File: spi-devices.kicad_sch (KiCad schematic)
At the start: 15 parts, among them U5 IIM-42652, U8 ICE5LP1K-SG48

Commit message: Checkpoint
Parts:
- C26: value (none) -> C_10u_0603; footprint (none) -> jetson-nano-baseboard-footprints:0603-cap
- C27: value (none) -> C_100n_0402; footprint (none) -> jetson-nano-baseboard-footprints:0402-cap
- D7: value (none) -> diode
- FB4: value (none) -> 100; footprint (none) -> jetson-nano-baseboard-footprints:0603-res
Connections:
- net IMU-INT1: now also U8.9 (IOB_16a)
- net IMU-INT2: now also U8.6 (IOB_13b)
- net SPI-CIPO: no longer U8.16 (IOB_35b_SPI_SS)
- net SPI-COPI: now also U8.17 (IOB_33b_SPI_SI)
- net SPI-SCK: now also U8.15 (IOB_34a_SPI_SCK); no longer U8.17 (IOB_33b_SPI_SI)
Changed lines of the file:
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@@
+    (stroke (width 0) (type default) (color 0 0 0 0))
+  )
+  (wire (pts (xy 226.06 90.17) (xy 232.41 90.17))
     (stroke (width 0) (type default) (color 0 0 0 0))
   )
@@
     (stroke (width 0) (type default) (color 0 0 0 0))
   )
+  (wire (pts (xy 215.9 59.69) (xy 232.41 59.69))
+    (stroke (width 0) (type default) (color 0 0 0 0))
+  )
   (wire (pts (xy 229.87 137.16) (xy 246.38 137.16))
     (stroke (width 0) (type default) (color 0 0 0 0))
@@
     (stroke (width 0) (type default) (color 0 0 0 0))
   )
-  (wire (pts (xy 44.45 68.58) (xy 52.07 68.58))
+  (wire (pts (xy 35.56 68.58) (xy 52.07 68.58))
+    (stroke (width 0) (type default) (color 0 0 0 0))
+  )
+  (wire (pts (xy 226.06 87.63) (xy 232.41 87.63))
     (stroke (width 0) (type default) (color 0 0 0 0))
   )
@@
     (stroke (width 0) (type default) (color 0 0 0 0))
   )
-  (wire (pts (xy 44.45 71.12) (xy 52.07 71.12))
+  (wire (pts (xy 35.56 71.12) (xy 52.07 71.12))
     (stroke (width 0) (type default) (color 0 0 0 0))
   )
@@
     (stroke (width 0) (type default) (color 0 0 0 0))
   )
+  (wire (pts (xy 215.9 62.23) (xy 232.41 62.23))
+    (stroke (width 0) (type default) (color 0 0 0 0))
+  )
   (wire (pts (xy 80.01 58.42) (xy 74.93 58.42))
     (stroke (width 0) (type default) (color 0 0 0 0))
@@
     (stroke (width 0) (type default) (color 0 0 0 0))
   )
-  (wire (pts (xy 226.06 87.63) (xy 232.41 87.63))
-    (stroke (width 0) (type default) (color 0 0 0 0))
-  )
   (wire (pts (xy 242.316 134.62) (xy 242.316 139.7))
     (stroke (width 0) (type default) (color 0 0 0 0))
@@
   (wire (pts (xy 235.712 134.62) (xy 242.316 134.62))
     (stroke (width 0) (type default) (color 0 0 0 0))
+  )
+  (label "IMU-INT2" (at 215.9 59.69 0)
+    (effects (font (size 1.27 1.27)) (justify left bottom))
+  )
+  (label "IMU-INT1" (at 215.9 62.23 0)
+    (effects (font (size 1.27 1.27)) (justify left bottom))
+  )
+  (label "IMU-INT2" (at 35.56 71.12 0)
+    (effects (font (size 1.27 1.27)) (justify left bottom))
   )
   (label "VCCPLL" (at 237.236 134.62 0)
     (effects (font (size 1.27 1.27)) (justify left bottom))
   )
+  (label "IMU-INT1" (at 35.56 68.58 0)
+    (effects (font (size 1.27 1.27)) (justify left bottom))
+  )
   (label "VPP2V5" (at 245.618 154.94 0)
     (effects (font (size 1.27 1.27)) (justify left bottom))
-  )
-  (global_label "IMU-INT1" (shape bidirectional) (at 44.45 68.58 180) (fields_autoplaced)
-    (effects (font (size 1.27 1.27)) (justify right))
-    (property "Intersheet References" "${INTERSHEET_REFS}" (id 0) (at 33.0544 68.5006 0)
-      (effects (font (size 1.27 1.27)) (justify right) hide)
-    )
   )
   (global_label "SPI-CIPO" (shape input) (at 44.45 55.88 180) (fields_autoplaced)
@@
     )
   )
-  (global_label "SPI-SCK" (shape input) (at 226.06 87.63 180) (fields_autoplaced)
-    (effects (font (size 1.27 1.27)) (justify right))
-    (property "Intersheet References" "${INTERSHEET_REFS}" (id 0) (at 215.3296 87.5506 0)
+  (global_label "SPI-SCK" (shape input) (at 226.06 90.17 180) (fields_autoplaced)
+    (effects (font (size 1.27 1.27)) (justify right))
+    (property "Intersheet References" "${INTERSHEET_REFS}" (id 0) (at 215.3296 90.0906 0)
       (effects (font (size 1.27 1.27)) (justify right) hide)
     )
@@
     )
   )
-  (global_label "CAM4-IO0" (shape output) (at 225.044 61.976 180) (fields_autoplaced)
-    (effects (font (size 1.27 1.27)) (justify right))
-    (property "Intersheet References" "${INTERSHEET_REFS}" (id 0) (at 212.9831 61.8966 0)
+  (global_label "CAM4-IO0" (shape output) (at 226.314 67.818 180) (fields_autoplaced)
+    (effects (font (size 1.27 1.27)) (justify right))
+    (property "Intersheet References" "${INTERSHEET_REFS}" (id 0) (at 214.2531 67.7386 0)
       (effects (font (size 1.27 1.27)) (justify right) hide)
     )
@@
     )
   )
-  (global_label "IMU-INT2" (shape bidirectional) (at 44.45 71.12 180) (fields_autoplaced)
-    (effects (font (size 1.27 1.27)) (justify right))
-    (property "Intersheet References" "${INTERSHEET_REFS}" (id 0) (at 33.0544 71.0406 0)
-      (effects (font (size 1.27 1.27)) (justify right) hide)
-    )
-  )
   (global_label "SPI-SCK" (shape input) (at 44.45 60.96 180) (fields_autoplaced)
     (effects (font (size 1.27 1.27)) (justify right))
@@
     )
   )
-  (global_label "SPI-CIPO" (shape input) (at 226.0912 92.71 180) (fields_autoplaced)
-    (effects (font (size 1.27 1.27)) (justify right))
-    (property "Intersheet References" "${INTERSHEET_REFS}" (id 0) (at 214.6351 92.6306 0)
+  (global_label "SPI-COPI" (shape input) (at 226.06 87.63 180) (fields_autoplaced)
+    (effects (font (size 1.27 1.27)) (justify right))
+    (property "Intersheet References" "${INTERSHEET_REFS}" (id 0) (at 214.6039 87.5506 0)
       (effects (font (size 1.27 1.27)) (justify right) hide)
     )
@@
     )
   )
-  (global_label "CAM4-IO1" (shape output) (at 225.044 64.516 180) (fields_autoplaced)
-    (effects (font (size 1.27 1.27)) (justify right))
-    (property "Intersheet References" "${INTERSHEET_REFS}" (id 0) (at 212.9831 64.4366 0)
+  (global_label "CAM4-IO1" (shape output) (at 226.314 70.358 180) (fields_autoplaced)
+    (effects (font (size 1.27 1.27)) (justify right))
+    (property "Intersheet References" "${INTERSHEET_REFS}" (id 0) (at 214.2531 70.2786 0)
       (effects (font (size 1.27 1.27)) (justify right) hide)
     )
@@
       (effects (font (size 1.524 1.524)) (justify left))
     )
-    (property "Value" "" (id 1) (at 242.316 139.7 0)
-      (effects (font (size 1.524 1.524)) hide)
-    )
-    (property "Footprint" "" (id 2) (at 237.236 148.59 0)
+    (property "Value" "C_100n_0402" (id 1) (at 242.316 139.7 0)
+      (effects (font (size 1.524 1.524)) hide)
+    )
+    (property "Footprint" "jetson-nano-baseboard-footprints:0402-cap" (id 2) (at 237.236 148.59 0)
       (effects (font (size 1.524 1.524)) (justify left) hide)
     )
@@
       (effects (font (size 1.524 1.524)) (justify left))
     )
-    (property "Value" "" (id 1) (at 235.712 139.7 0)
-      (effects (font (size 1.524 1.524)) hide)
-    )
-    (property "Footprint" "" (id 2) (at 230.632 148.59 0)
+    (property "Value" "C_10u_0603" (id 1) (at 235.712 139.7 0)
+      (effects (font (size 1.524 1.524)) hide)
+    )
+    (property "Footprint" "jetson-nano-baseboard-footprints:0603-cap" (id 2) (at 230.632 148.59 0)
       (effects (font (size 1.524 1.524)) (justify left) hide)
     )
@@
       (effects (font (size 1.524 1.524)))
     )
-    (property "Value" "" (id 1) (at 242.824 156.464 90)
+    (property "Value" "diode" (id 1) (at 242.824 156.464 90)
       (effects (font (size 1.524 1.524)))
     )
@@
     (in_bom yes) (on_board yes)
     (property "Reference" "FB4" (id 0) (at 225.0059 133.35 90))
-    (property "Value" "" (id 1) (at 230.8479 133.604 90))
-    (property "Footprint" "" (id 2) (at 227.33 136.398 90)
-      (effects (font (size 1.27 1.27)) hide)
-    )
+    (property "Value" "100" (id 1) (at 230.8479 133.604 90))
+    (property "Footprint" "jetson-nano-baseboard-footprints:0603-res" (id 2) (at 227.33 136.398 90)
+      (effects (font (size 1.27 1.27)) hide)
+    )

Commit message: Checkpoint
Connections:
- net CAM0-IO0: now also U8.44 (IOB_3b_G6); no longer U8.46 (IOB_0a)
- net CAM0-IO1: now also U8.45 (IOB_5b); no longer U8.47 (IOB_2a)
- net CAM1-IO0: now also U8.47 (IOB_2a); no longer U8.44 (IOB_3b_G6)
- net CAM1-IO1: now also U8.46 (IOB_0a); no longer U8.48 (IOB_4a)
- net CAM2-IO0: now also U8.4 (IOB_8a); no longer U8.45 (IOB_5b)
- net CAM2-IO1: now also U8.3 (IOB_9b); no longer U8.2 (IOB_6a)
- net CAM3-IO0: now also U8.2 (IOB_6a); no longer U8.4 (IOB_8a)
- net CAM3-IO1: now also U8.48 (IOB_4a); no longer U8.3 (IOB_9b)
- net CAM4-IO0: now also U8.9 (IOB_16a)
- net CAM4-IO1: now also U8.10 (IOB_18a)
- net IMU-INT1: now also U8.12 (IOB_22b); no longer U8.9 (IOB_16a)
- net IMU-INT2: now also U8.11 (IOB_20a); no longer U8.6 (IOB_13b)
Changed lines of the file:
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@@
+    (stroke (width 0) (type default) (color 0 0 0 0))
+  )
+  (wire (pts (xy 222.504 64.77) (xy 232.41 64.77))
     (stroke (width 0) (type default) (color 0 0 0 0))
   )
@@
     (stroke (width 0) (type default) (color 0 0 0 0))
   )
+  (wire (pts (xy 222.504 62.23) (xy 232.41 62.23))
+    (stroke (width 0) (type default) (color 0 0 0 0))
+  )
   (wire (pts (xy 97.155 52.705) (xy 97.155 54.61))
     (stroke (width 0) (type default) (color 0 0 0 0))
@@
     (stroke (width 0) (type default) (color 0 0 0 0))
   )
-  (wire (pts (xy 215.9 59.69) (xy 232.41 59.69))
+  (wire (pts (xy 223.012 67.31) (xy 232.41 67.31))
     (stroke (width 0) (type default) (color 0 0 0 0))
   )
@@
     (stroke (width 0) (type default) (color 0 0 0 0))
   )
-  (wire (pts (xy 215.9 62.23) (xy 232.41 62.23))
+  (wire (pts (xy 223.012 69.85) (xy 232.41 69.85))
     (stroke (width 0) (type default) (color 0 0 0 0))
   )
@@
     (stroke (width 0) (type default) (color 0 0 0 0))
   )
-  (label "IMU-INT2" (at 215.9 59.69 0)
-    (effects (font (size 1.27 1.27)) (justify left bottom))
-  )
-  (label "IMU-INT1" (at 215.9 62.23 0)
+  (label "IMU-INT2" (at 223.012 67.31 0)
+    (effects (font (size 1.27 1.27)) (justify left bottom))
+  )
+  (label "IMU-INT1" (at 223.012 69.85 0)
     (effects (font (size 1.27 1.27)) (justify left bottom))
   )
@@
     )
   )
-  (global_label "CAM2-IO0" (shape output) (at 167.64 133.35 180) (fields_autoplaced)
-    (effects (font (size 1.27 1.27)) (justify right))
-    (property "Intersheet References" "${INTERSHEET_REFS}" (id 0) (at 155.5791 133.2706 0)
-      (effects (font (size 1.27 1.27)) (justify right) hide)
-    )
-  )
-  (global_label "CAM3-IO1" (shape output) (at 167.64 140.97 180) (fields_autoplaced)
-    (effects (font (size 1.27 1.27)) (justify right))
-    (property "Intersheet References" "${INTERSHEET_REFS}" (id 0) (at 155.5791 140.8906 0)
-      (effects (font (size 1.27 1.27)) (justify right) hide)
-    )
-  )
-  (global_label "CAM3-IO0" (shape output) (at 167.64 138.43 180) (fields_autoplaced)
+  (global_label "CAM2-IO0" (shape output) (at 167.64 138.43 180) (fields_autoplaced)
     (effects (font (size 1.27 1.27)) (justify right))
     (property "Intersheet References" "${INTERSHEET_REFS}" (id 0) (at 155.5791 138.3506 0)
+      (effects (font (size 1.27 1.27)) (justify right) hide)
+    )
+  )
+  (global_label "CAM3-IO1" (shape output) (at 167.64 130.81 180) (fields_autoplaced)
+    (effects (font (size 1.27 1.27)) (justify right))
+    (property "Intersheet References" "${INTERSHEET_REFS}" (id 0) (at 155.5791 130.7306 0)
+      (effects (font (size 1.27 1.27)) (justify right) hide)
+    )
+  )
+  (global_label "CAM3-IO0" (shape output) (at 167.64 135.89 180) (fields_autoplaced)
+    (effects (font (size 1.27 1.27)) (justify right))
+    (property "Intersheet References" "${INTERSHEET_REFS}" (id 0) (at 155.5791 135.8106 0)
       (effects (font (size 1.27 1.27)) (justify right) hide)
     )
@@
     )
   )
-  (global_label "CAM4-IO0" (shape output) (at 226.314 67.818 180) (fields_autoplaced)
-    (effects (font (size 1.27 1.27)) (justify right))
-    (property "Intersheet References" "${INTERSHEET_REFS}" (id 0) (at 214.2531 67.7386 0)
-      (effects (font (size 1.27 1.27)) (justify right) hide)
-    )
-  )
-  (global_label "CAM2-IO1" (shape output) (at 167.64 135.89 180) (fields_autoplaced)
-    (effects (font (size 1.27 1.27)) (justify right))
-    (property "Intersheet References" "${INTERSHEET_REFS}" (id 0) (at 155.5791 135.8106 0)
+  (global_label "CAM4-IO0" (shape output) (at 222.504 62.23 180) (fields_autoplaced)
+    (effects (font (size 1.27 1.27)) (justify right))
+    (property "Intersheet References" "${INTERSHEET_REFS}" (id 0) (at 210.4431 62.1506 0)
+      (effects (font (size 1.27 1.27)) (justify right) hide)
+    )
+  )
+  (global_label "CAM2-IO1" (shape output) (at 167.64 140.97 180) (fields_autoplaced)
+    (effects (font (size 1.27 1.27)) (justify right))
+    (property "Intersheet References" "${INTERSHEET_REFS}" (id 0) (at 155.5791 140.8906 0)
       (effects (font (size 1.27 1.27)) (justify right) hide)
     )
@@
     )
   )
-  (global_label "CAM0-IO0" (shape output) (at 167.64 123.19 180) (fields_autoplaced)
+  (global_label "CAM0-IO0" (shape output) (at 167.64 128.27 180) (fields_autoplaced)
+    (effects (font (size 1.27 1.27)) (justify right))
+    (property "Intersheet References" "${INTERSHEET_REFS}" (id 0) (at 155.5791 128.1906 0)
+      (effects (font (size 1.27 1.27)) (justify right) hide)
+    )
+  )
+  (global_label "CAM-VIO" (shape input) (at 180.34 106.68 180) (fields_autoplaced)
+    (effects (font (size 1.27 1.27)) (justify right))
+    (property "Intersheet References" "${INTERSHEET_REFS}" (id 0) (at 169.6096 106.7594 0)
+      (effects (font (size 1.27 1.27)) (justify right) hide)
+    )
+  )
+  (global_label "ICE-RESET" (shape input) (at 226.06 52.07 180) (fields_autoplaced)
+    (effects (font (size 1.27 1.27)) (justify right))
+    (property "Intersheet References" "${INTERSHEET_REFS}" (id 0) (at 213.3944 51.9906 0)
+      (effects (font (size 1.27 1.27)) (justify right) hide)
+    )
+  )
+  (global_label "3V3_SYS" (shape input) (at 226.06 38.1 180) (fields_autoplaced)
+    (effects (font (size 1.27 1.27)) (justify right))
+    (property "Intersheet References" "${INTERSHEET_REFS}" (id 0) (at 215.7529 38.0206 0)
+      (effects (font (size 1.27 1.27)) (justify right) hide)
+    )
+  )
+  (global_label "SPI-COPI" (shape input) (at 226.06 87.63 180) (fields_autoplaced)
+    (effects (font (size 1.27 1.27)) (justify right))
+    (property "Intersheet References" "${INTERSHEET_REFS}" (id 0) (at 214.6039 87.5506 0)
+      (effects (font (size 1.27 1.27)) (justify right) hide)
+    )
+  )
+  (global_label "CAM1-IO0" (shape output) (at 167.64 125.73 180) (fields_autoplaced)
+    (effects (font (size 1.27 1.27)) (justify right))
+    (property "Intersheet References" "${INTERSHEET_REFS}" (id 0) (at 155.5791 125.6506 0)
+      (effects (font (size 1.27 1.27)) (justify right) hide)
+    )
+  )
+  (global_label "SPI-CS1" (shape input) (at 226.06 74.93 180) (fields_autoplaced)
+    (effects (font (size 1.27 1.27)) (justify right))
+    (property "Intersheet References" "${INTERSHEET_REFS}" (id 0) (at 215.3901 74.8506 0)
+      (effects (font (size 1.27 1.27)) (justify right) hide)
+    )
+  )
+  (global_label "CAM4-IO1" (shape output) (at 222.504 64.77 180) (fields_autoplaced)
+    (effects (font (size 1.27 1.27)) (justify right))
+    (property "Intersheet References" "${INTERSHEET_REFS}" (id 0) (at 210.4431 64.6906 0)
+      (effects (font (size 1.27 1.27)) (justify right) hide)
+    )
+  )
+  (global_label "CAM1-IO1" (shape output) (at 167.64 123.19 180) (fields_autoplaced)
     (effects (font (size 1.27 1.27)) (justify right))
     (property "Intersheet References" "${INTERSHEET_REFS}" (id 0) (at 155.5791 123.1106 0)
@@
     )
   )
-  (global_label "CAM-VIO" (shape input) (at 180.34 106.68 180) (fields_autoplaced)
-    (effects (font (size 1.27 1.27)) (justify right))
-    (property "Intersheet References" "${INTERSHEET_REFS}" (id 0) (at 169.6096 106.7594 0)
-      (effects (font (size 1.27 1.27)) (justify right) hide)
-    )
-  )
-  (global_label "ICE-RESET" (shape input) (at 226.06 52.07 180) (fields_autoplaced)
-    (effects (font (size 1.27 1.27)) (justify right))
-    (property "Intersheet References" "${INTERSHEET_REFS}" (id 0) (at 213.3944 51.9906 0)
-      (effects (font (size 1.27 1.27)) (justify right) hide)
-    )
-  )
-  (global_label "3V3_SYS" (shape input) (at 226.06 38.1 180) (fields_autoplaced)
-    (effects (font (size 1.27 1.27)) (justify right))
-    (property "Intersheet References" "${INTERSHEET_REFS}" (id 0) (at 215.7529 38.0206 0)
-      (effects (font (size 1.27 1.27)) (justify right) hide)
-    )
-  )
-  (global_label "SPI-COPI" (shape input) (at 226.06 87.63 180) (fields_autoplaced)
-    (effects (font (size 1.27 1.27)) (justify right))
-    (property "Intersheet References" "${INTERSHEET_REFS}" (id 0) (at 214.6039 87.5506 0)
-      (effects (font (size 1.27 1.27)) (justify right) hide)
-    )
-  )
-  (global_label "CAM1-IO0" (shape output) (at 167.64 128.27 180) (fields_autoplaced)
-    (effects (font (size 1.27 1.27)) (justify right))
-    (property "Intersheet References" "${INTERSHEET_REFS}" (id 0) (at 155.5791 128.1906 0)
-      (effects (font (size 1.27 1.27)) (justify right) hide)
-    )
-  )
-  (global_label "SPI-CS1" (shape input) (at 226.06 74.93 180) (fields_autoplaced)
-    (effects (font (size 1.27 1.27)) (justify right))
-    (property "Intersheet References" "${INTERSHEET_REFS}" (id 0) (at 215.3901 74.8506 0)
-      (effects (font (size 1.27 1.27)) (justify right) hide)
-    )
-  )
-  (global_label "CAM4-IO1" (shape output) (at 226.314 70.358 180) (fields_autoplaced)
-    (effects (font (size 1.27 1.27)) (justify right))
-    (property "Intersheet References" "${INTERSHEET_REFS}" (id 0) (at 214.2531 70.2786 0)
-      (effects (font (size 1.27 1.27)) (justify right) hide)
-    )
-  )
-  (global_label "CAM1-IO1" (shape output) (at 167.64 130.81 180) (fields_autoplaced)
-    (effects (font (size 1.27 1.27)) (justify right))
-    (property "Intersheet References" "${INTERSHEET_REFS}" (id 0) (at 155.5791 130.7306 0)
-      (effects (font (size 1.27 1.27)) (justify right) hide)
-    )
-  )
-  (global_label "CAM0-IO1" (shape output) (at 167.64 125.73 180) (fields_autoplaced)
-    (effects (font (size 1.27 1.27)) (justify right))
-    (property "Intersheet References" "${INTERSHEET_REFS}" (id 0) (at 155.5791 125.6506 0)
-      (effects (font (size 1.27 1.27)) (justify right) hide)
-    )
+  (global_label "CAM0-IO1" (shape output) (at 167.64 133.35 180) (fields_autoplaced)
+    (effects (font (size 1.27 1.27)) (justify right))
+    (property "Intersheet References" "${INTERSHEET_REFS}" (id 0) (at 155.5791 133.2706 0)
+      (effects (font (size 1.27 1.27)) (justify right) hide)
+    )

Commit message: Checkpoint
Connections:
- net CAM-VIO renamed CAM_VIO
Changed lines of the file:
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@@
     )
   )
-  (global_label "CAM-VIO" (shape input) (at 180.34 106.68 180) (fields_autoplaced)
+  (global_label "CAM_VIO" (shape input) (at 180.34 106.68 180) (fields_autoplaced)
     (effects (font (size 1.27 1.27)) (justify right))
-    (property "Intersheet References" "${INTERSHEET_REFS}" (id 0) (at 169.6096 106.7594 0)
+    (property "Intersheet References" "${INTERSHEET_REFS}" (id 0) (at 170.2144 106.6006 0)
       (effects (font (size 1.27 1.27)) (justify right) hide)
     )

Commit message: Checkpoint
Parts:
- added C3, C4, C5: C_2u2_0402, jetson-nano-baseboard-footprints:0402-cap, symbol jetson-nano-baseboard:C_2u2_0402
- added C6, C7: C_1u_0402, jetson-nano-baseboard-footprints:0402-cap, symbol jetson-nano-baseboard:C_1u_0402
- added IC5, IC6: (no value), symbol jetson-nano-baseboard:TPS7A0518PDBVT
- added R52: R_10k_0402, jetson-nano-baseboard-footprints:0402-res, symbol jetson-nano-baseboard:R_10k_0402
- added TP3, TP5: ~, jetson-nano-baseboard-footprints:TP-R-1.5, symbol jetson-nano-baseboard:Testpad
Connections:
- net 3V3_SYS: no longer C23.2, C33.2, D7.A, R31.2, U8.22 (SPI_VCCIO1)
- net GND: now also C3.2, C4.2, C5.2, C6.2, C7.2, IC5.2 (GND), IC6.2 (GND)
- net 3V3_ICE: now reaches U8.33 (VCCIO_0)
- net 3V3_ICE: now also C23.2, C33.2, D7.A, R31.2, U8.22 (SPI_VCCIO1), C7.1, IC6.5 (VOUT), TP5.1 (P)
- net 1V2_SYS renamed 1V2_ICE
- net 1V2_ICE: now also C6.1, IC5.5 (VOUT), TP3.1 (P)
- new net: C5.1, IC6.3 (EN), R52.1
- new net 5V0_SYS: C3.1, C4.1, IC5.1 (VIN), IC5.3 (EN), IC6.1 (VIN), R52.2
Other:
- note added: "FPGA 1v2"
- note added: "FPGA 3v3"

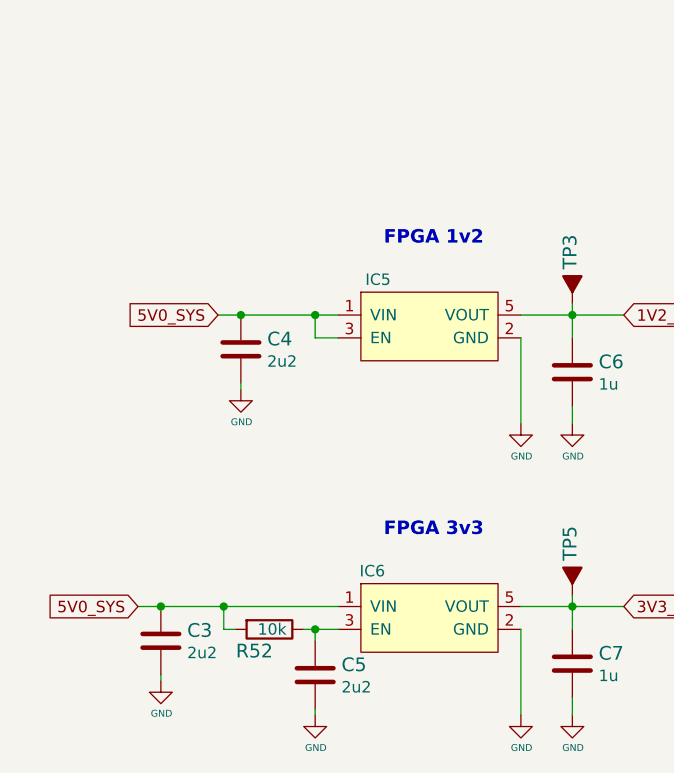
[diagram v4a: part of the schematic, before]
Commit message: Change 3v regulator. More layout
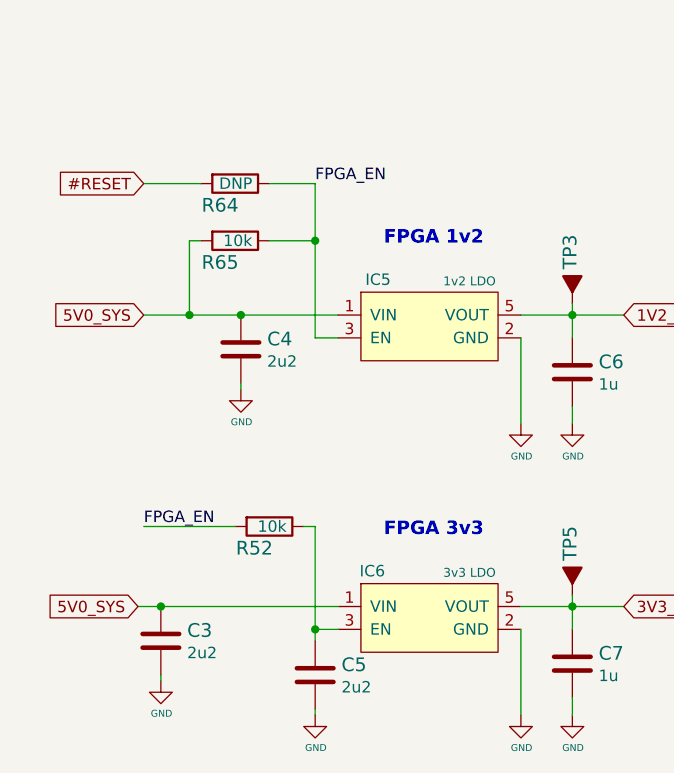
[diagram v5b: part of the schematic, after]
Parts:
- added R64, R65: R_10k_0402, jetson-nano-baseboard-footprints:0402-res, symbol jetson-nano-baseboard:R_10k_0402
- IC5: value (none) -> 1v2 LDO; footprint (none) -> jetson-nano-baseboard-footprints:SOT-23-5
- IC6: value (none) -> 3v3 LDO; footprint (none) -> jetson-nano-baseboard-footprints:SOT-23-5
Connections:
- net 5V0_SYS: now also R65.2; no longer IC5.3 (EN), R52.2
- new net #RESET: R64.2
- new net FPGA_EN: IC5.3 (EN), R52.2, R64.1, R65.1
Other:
- moved on the sheet: R52
